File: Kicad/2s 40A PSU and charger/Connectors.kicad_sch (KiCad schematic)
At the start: 19 parts, among them J1 Keystone 3579, J10 USB_C_Receptacle_USB2.0_16P, J11 1.27mm 4 pin socket, J2 JST XH-S Balance Plug, J3 Keystone 3579, J4 Keystone 3569, J5 Keystone 3569, J6 Keystone 3579, J7 Keystone 3579, J8 Keystone 3569, J9 Keystone 3569

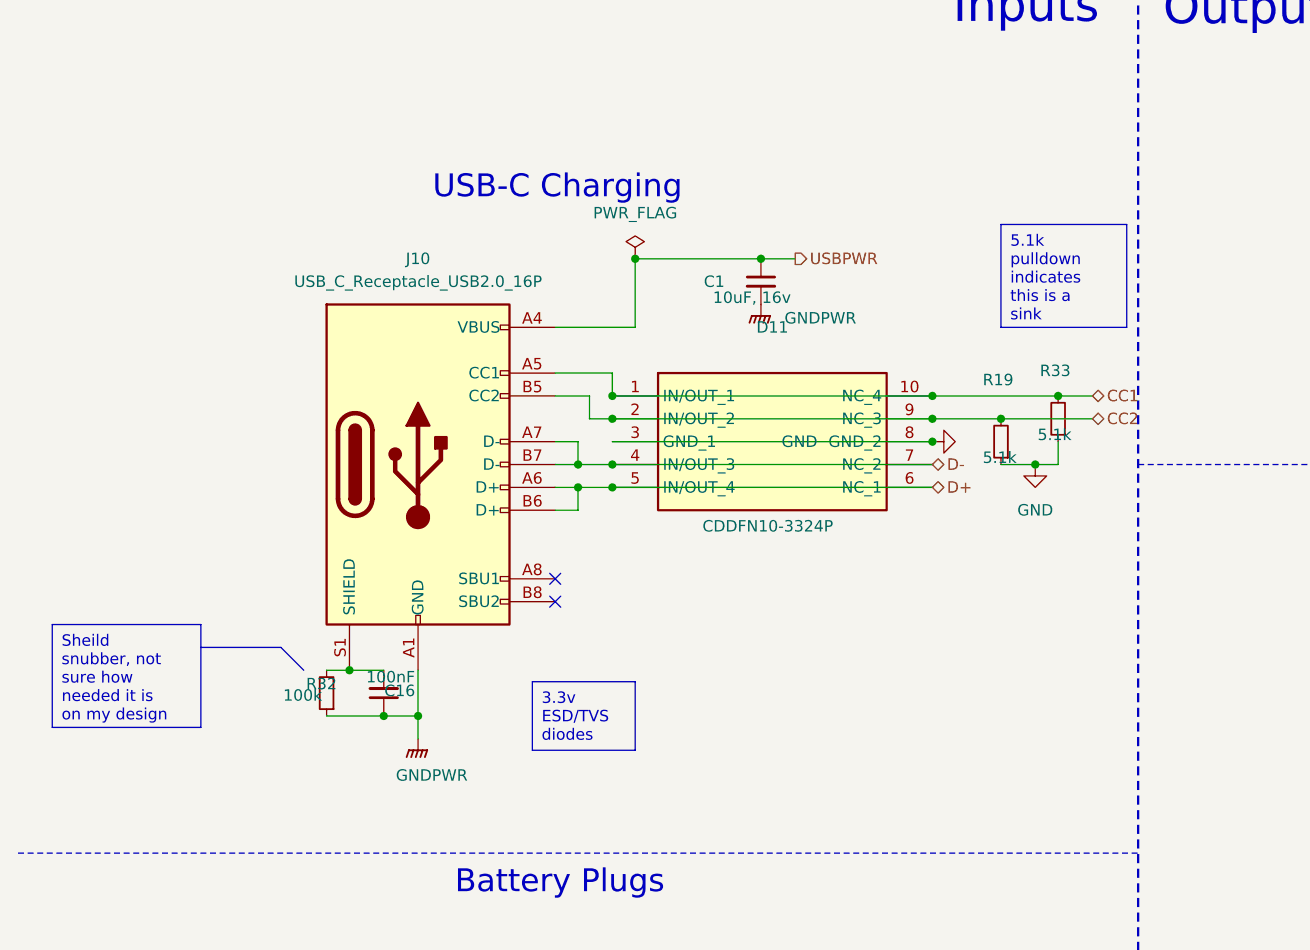
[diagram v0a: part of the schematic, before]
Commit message: Added TVS diodes for USB-C
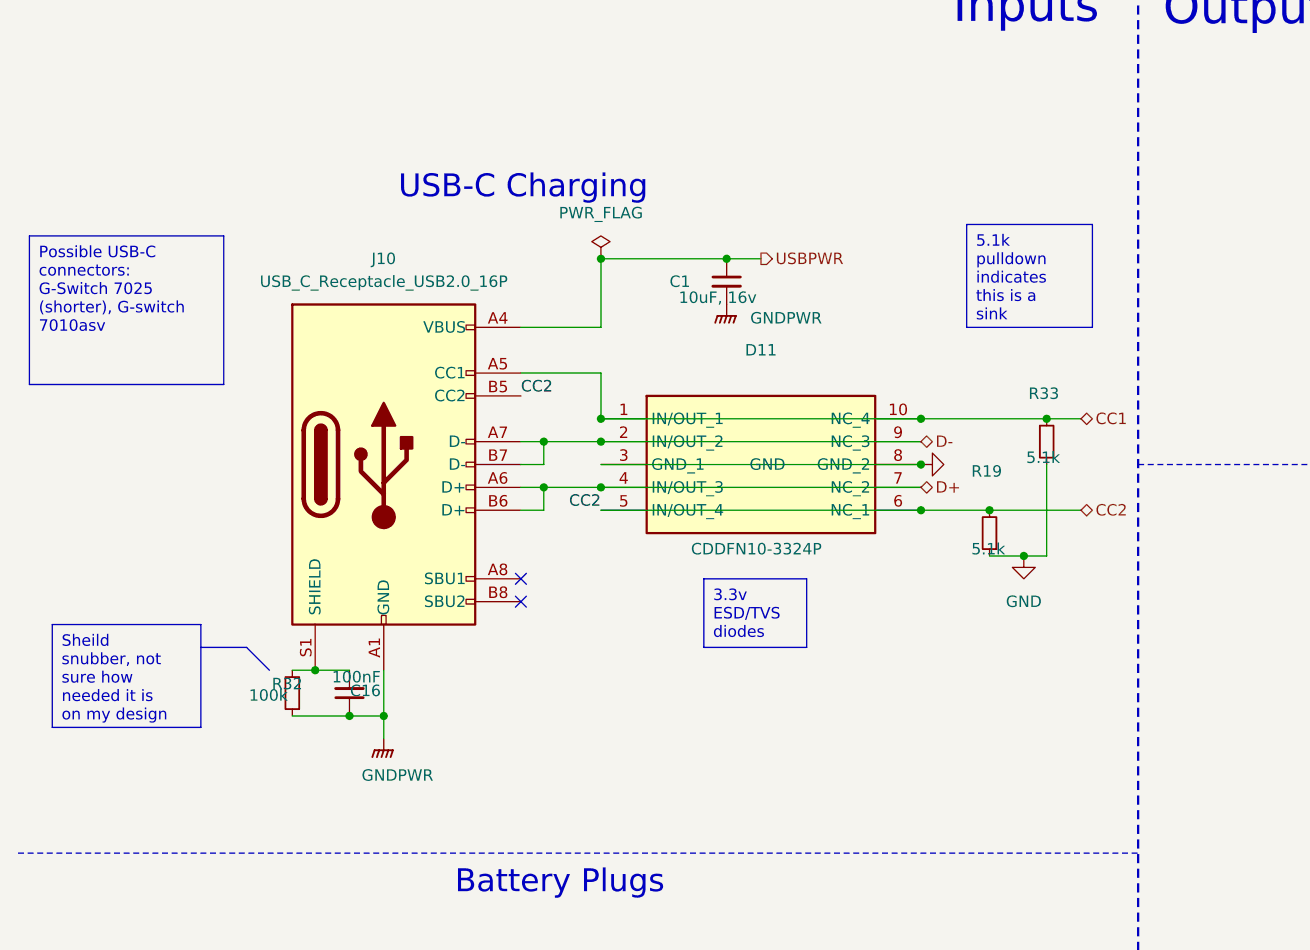
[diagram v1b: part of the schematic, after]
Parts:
- J10: footprint Connector_USB:USB_C_Receptacle_XKB_U262-16XN-4BVC11 -> Connector_USB:USB_C_Receptacle_G-Switch_GT-USB-7025
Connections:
- net CC2: now also D11.5 (IN/OUT_4), D11.6 (NC_1); no longer D11.2 (IN/OUT_2), D11.9 (NC_3)
- net D+: now also D11.4 (IN/OUT_3), D11.7 (NC_2); no longer D11.5 (IN/OUT_4), D11.6 (NC_1)
- net D-: now also D11.2 (IN/OUT_2), D11.9 (NC_3); no longer D11.4 (IN/OUT_3), D11.7 (NC_2)
- net GNDPWR: now also J10.GND
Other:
- moved on the sheet: C1, C16, D11, J10, R19, R32, R33

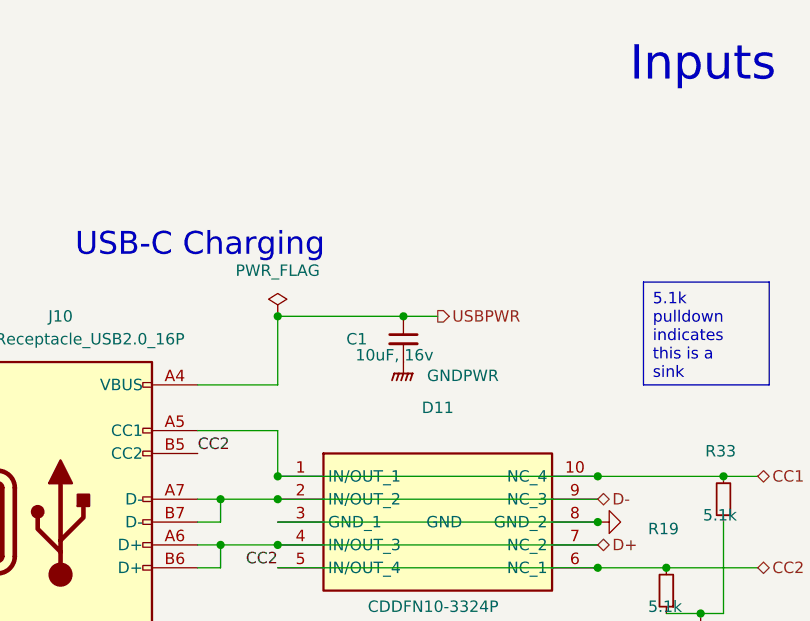
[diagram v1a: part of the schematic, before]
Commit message: Merged Always on PWR for multiple devices
The diode OR and the 10 ohm resistor are now shared between the MCU and the battery charger
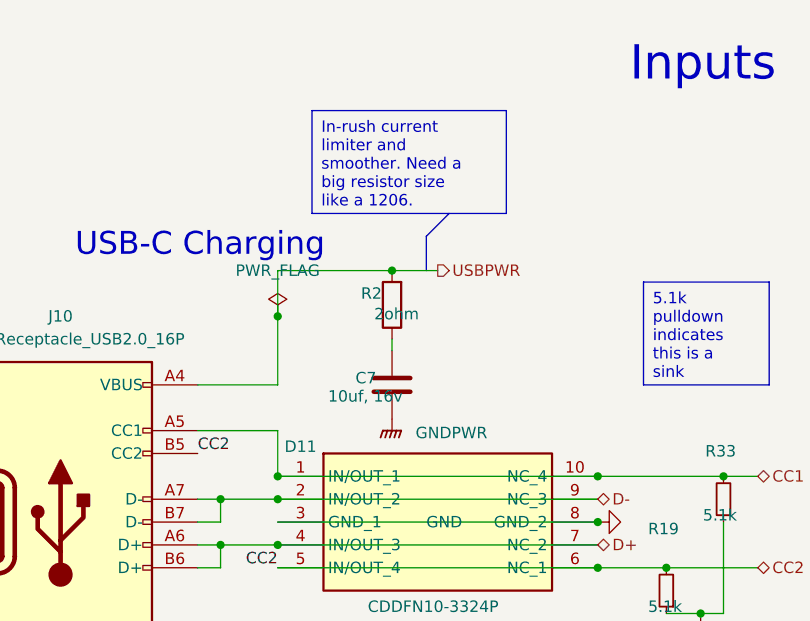
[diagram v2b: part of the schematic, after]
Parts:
- removed C1: 10uF, 16v, Capacitor_SMD:C_0805_2012Metric, symbol Device:C_Small
- added C7: 10uf, 16v, Capacitor_SMD:C_0805_2012Metric, symbol Device:C
- added R2: 2ohm, Resistor_SMD:R_0805_2012Metric, symbol Device:R
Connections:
- net GNDPWR: now also C7.2
- net USBPWR: now also R2.2
- new net: C7.1, R2.1
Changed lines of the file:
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@@
 	)
 	(junction
-		(at 90.17 44.45)
+		(at 68.58 163.83)
 		(diameter 0)
 		(color 0 0 0 0)
 	)
 	(junction
-		(at 68.58 163.83)
+		(at 88.9 39.37)
 		(diameter 0)
 		(color 0 0 0 0)
@@
 	(wire
 		(pts
-			(xy 90.17 44.45) (xy 93.98 44.45)
-		)
-		(stroke
-			(width 0)
-			(type default)
-		)
-	)
-	(wire
-		(pts
 			(xy 201.93 91.44) (xy 201.93 95.25)
 		)
@@
 	(wire
 		(pts
-			(xy 76.2 44.45) (xy 90.17 44.45)
+			(xy 76.2 39.37) (xy 88.9 39.37)
 		)
 		(stroke
@@
 	(wire
 		(pts
+			(xy 88.9 48.26) (xy 88.9 46.99)
+		)
+		(stroke
+			(width 0)
+			(type default)
+		)
+	)
+	(wire
+		(pts
 			(xy 69.85 64.77) (xy 69.85 67.31)
 		)
@@
 		)
 	)
+	(polyline
+		(pts
+			(xy 92.71 35.56) (xy 95.25 33.02)
+		)
+		(stroke
+			(width 0)
+			(type default)
+		)
+	)
 	(wire
 		(pts
@@
 		)
 	)
+	(polyline
+		(pts
+			(xy 92.71 39.37) (xy 92.71 35.56)
+		)
+		(stroke
+			(width 0)
+			(type default)
+		)
+	)
+	(wire
+		(pts
+			(xy 76.2 39.37) (xy 76.2 44.45)
+		)
+		(stroke
+			(width 0)
+			(type default)
+		)
+	)
 	(wire
 		(pts
@@
 	(wire
 		(pts
+			(xy 88.9 39.37) (xy 93.98 39.37)
+		)
+		(stroke
+			(width 0)
+			(type default)
+		)
+	)
+	(wire
+		(pts
 			(xy 201.93 140.97) (xy 203.2 140.97)
 		)
@@
 		)
 	)
+	(text_box "In-rush current limiter and smoother. Need a big resistor size like a 1206."
+		(exclude_from_sim no)
+		(at 80.01 21.59 0)
+		(size 21.59 11.43)
+		(stroke
+			(width 0)
+			(type default)
+		)
+		(fill
+			(type none)
+		)
+		(effects
+			(font
+				(size 1.27 1.27)
+			)
+			(justify left top)
+		)
+	)
 	(text_box "5.1k pulldown indicates this is a sink"
 		(exclude_from_sim no)
@@
 	(hierarchical_label "USBPWR"
 		(shape output)
-		(at 93.98 44.45 0)
+		(at 93.98 39.37 0)
 		(fields_autoplaced yes)
 		(effects
@@
 		)
 		(property "Netclass" "USB-C pwr"
-			(at 93.98 45.72 0)
+			(at 93.98 40.64 0)
 			(effects
 				(font
@@
 		)
 	)
+	(netclass_flag ""
+		(length 2.54)
+		(shape round)
+		(at 114.3 62.23 0)
+		(fields_autoplaced yes)
+		(effects
+			(font
+				(size 1.27 1.27)
+			)
+			(justify left bottom)
+		)
+		(property "Netclass" "Default"
+			(at 114.9985 59.69 0)
+			(effects
+				(font
+					(size 1.27 1.27)
+					(italic yes)
+				)
+				(justify left)
+			)
+		)
+	)
+	(netclass_flag ""
+		(length 2.54)
+		(shape round)
+		(at 123.19 72.39 0)
+		(fields_autoplaced yes)
+		(effects
+			(font
+				(size 1.27 1.27)
+			)
+			(justify left bottom)
+		)
+		(property "Netclass" "Default"
+			(at 123.8885 69.85 0)
+			(effects
+				(font
+					(size 1.27 1.27)
+					(italic yes)
+				)
+				(justify left)
+			)
+		)
+	)
+	(netclass_flag ""
+		(length 2.54)
+		(shape round)
+		(at 88.9 48.26 270)
+		(effects
+			(font
+				(size 1.27 1.27)
+			)
+			(justify right bottom)
+		)
+		(property "Netclass" "USB-C pwr"
+			(at 93.472 48.26 0)
+			(effects
+				(font
+					(size 1.27 1.27)
+					(italic yes)
+				)
+				(justify left)
+			)
+		)
+	)
 	(symbol
 		(lib_id "power:GNDPWR")
@@
 	(symbol
 		(lib_id "power:GNDPWR")
-		(at 90.17 49.53 0)
+		(at 88.9 55.88 0)
 		(unit 1)
 		(exclude_from_sim no)
@@
 		(dnp no)
 		(property "Reference" "#PWR08"
-			(at 90.17 54.61 0)
+			(at 88.9 60.96 0)
 			(effects
 				(font
@@
 		)
 		(property "Value" "GNDPWR"
-			(at 96.774 51.054 0)
+			(at 95.504 57.404 0)
 			(effects
 				(font
@@
 		)
 		(property "Footprint" ""
-			(at 90.17 50.8 0)
+			(at 88.9 57.15 0)
 			(effects
 				(font
@@
 		)
 		(property "Datasheet" ""
-			(at 90.17 50.8 0)
+			(at 88.9 57.15 0)
 			(effects
 				(font
@@
 		)
 		(property "Description" "Power symbol creates a global label with name \"GNDPWR\" , global ground"
-			(at 90.17 49.53 0)
+			(at 88.9 55.88 0)
 			(effects
 				(font
@@
 	)
 	(symbol
+		(lib_id "Device:R")
+		(at 88.9 43.18 180)
+		(unit 1)
+		(exclude_from_sim no)
+		(in_bom yes)
+		(on_board yes)
+		(dnp no)
+		(property "Reference" "R2"
+			(at 86.614 41.91 0)
+			(effects
+				(font
+					(size 1.27 1.27)
+				)
+			)
+		)
+		(property "Value" "2ohm"
+			(at 89.408 44.196 0)
+			(effects
+				(font
+					(size 1.27 1.27)
+				)
+			)
+		)
+		(property "Footprint" "Resistor_SMD:R_0805_2012Metric"
+			(at 90.678 43.18 90)
+			(effects
+				(font
+					(size 1.27 1.27)
+				)
+				(hide yes)
+			)
+		)
+		(property "Datasheet" "~"
+			(at 88.9 43.18 0)
+			(effects
+				(font
+					(size 1.27 1.27)
+				)
+				(hide yes)
+			)
+		)
+		(property "Description" "Resistor"
+			(at 88.9 43.18 0)
+			(effects
+				(font
+					(size 1.27 1.27)
+				)
+				(hide yes)
+			)
+		)
+		(pin "2"
+		)
+		(pin "1"
+		)
+		(instances
+			(project "2s 40A PSU and charger"
+				(path "/eb3f183d-8bb1-43a5-a363-092ed67891e3/3a3003bc-8e40-4cd7-b859-421f37e4b48c"
+					(reference "R2")
+					(unit 1)
+				)
+			)
+		)
+	)
+	(symbol
 		(lib_id "Connector:Conn_01x01_Pin")
 		(at 208.28 105.41 180)
@@
 	)
 	(symbol
+		(lib_id "Device:C")
+		(at 88.9 52.07 0)
+		(unit 1)
+		(exclude_from_sim no)
+		(in_bom yes)
+		(on_board yes)
+		(dnp no)
+		(property "Reference" "C7"
+			(at 84.836 51.308 0)
+			(effects
+				(font
+					(size 1.27 1.27)
+				)
+				(justify left)
+			)
+		)
+		(property "Value" "10uf, 16v"
+			(at 81.788 53.34 0)
+			(effects
+				(font
+					(size 1.27 1.27)
+				)
+				(justify left)
+			)
+		)
+		(property "Footprint" "Capacitor_SMD:C_0805_2012Metric"
+			(at 89.8652 55.88 0)
+			(effects
+				(font
+					(size 1.27 1.27)
+				)
+				(hide yes)
+			)
+		)
+		(property "Datasheet" "~"
+			(at 88.9 52.07 0)
+			(effects
+				(font
+					(size 1.27 1.27)
+				)
+				(hide yes)
+			)
+		)
+		(property "Description" "Unpolarized capacitor"
+			(at 88.9 52.07 0)
+			(effects
+				(font
+					(size 1.27 1.27)
+				)
+				(hide yes)
+			)
+		)
+		(pin "1"
+		)
+		(pin "2"
+		)
+		(instances
+			(project "2s 40A PSU and charger"
+				(path "/eb3f183d-8bb1-43a5-a363-092ed67891e3/3a3003bc-8e40-4cd7-b859-421f37e4b48c"
+					(reference "C7")
+					(unit 1)
+				)
+			)
+		)
+	)
+	(symbol
 		(lib_id "Connector:Conn_01x01_Pin")
 		(at 208.28 137.16 180)
@@
 		(dnp no)
 		(property "Reference" "D11"
-			(at 93.98 54.61 0)
+			(at 78.74 58.928 0)
 			(effects
 				(font
@@
 					(unit 1)
 				)
-			)
-		)
-	)
-	(symbol
-		(lib_id "Device:C_Small")
-		(at 90.17 46.99 0)
-		(unit 1)
-		(exclude_from_sim no)
-		(in_bom yes)
-		(on_board yes)
-		(dnp no)
-		(property "Reference" "C1"
-			(at 83.82 46.99 0)
-			(effects
-				(font
-					(size 1.27 1.27)
-				)
-				(justify left)
-			)
-		)
-		(property "Value" "10uF, 16v"
-			(at 84.836 48.768 0)
-			(effects
-				(font
-					(size 1.27 1.27)
-				)
-				(justify left)
-			)
-		)
-		(property "Footprint" "Capacitor_SMD:C_0805_2012Metric"
-			(at 90.17 46.99 0)
-			(effects
-				(font
-					(size 1.27 1.27)
-				)
-				(hide yes)
-			)
-		)
-		(property "Datasheet" "~"
-			(at 90.17 46.99 0)
-			(effects
-				(font
-					(size 1.27 1.27)
-				)
-				(hide yes)
-			)
-		)
-		(property "Description" "Unpolarized capacitor, small symbol"
-			(at 90.17 46.99 0)
-			(effects
-				(font
-					(size 1.27 1.27)
-				)
-				(hide yes)
-			)
-		)
-		(pin "1"
-		)
-		(pin "2"
-		)
-		(instances
-			(project "2s 40A PSU and charger"
-				(path "/eb3f183d-8bb1-43a5-a363-092ed67891e3/3a3003bc-8e40-4cd7-b859-421f37e4b48c"
-					(reference "C1")
-					(unit 1)
-				)
-			)
-			(project "Connectors"
-				(path "/ef905b65-82b7-484f-997c-0c6089b83b28"
-					(reference "C?")
-					(unit 1)
-				)
